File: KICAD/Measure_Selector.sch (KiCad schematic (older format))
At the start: 1 part

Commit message: merge program breaker nicolas
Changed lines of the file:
@@
 	-1   0    0    -1
 $EndComp
-Wire Wire Line
-	4900 3800 5225 3800
-Wire Wire Line
-	4900 3900 5225 3900
-Wire Wire Line
-	4900 4100 5225 4100
-Wire Wire Line
-	4900 4200 5225 4200
 $Comp
 L power:GND #PWR?
@@
 Wire Wire Line
 	5250 4500 4850 4500
+Wire Wire Line
+	5250 3800 4900 3800
+Wire Wire Line
+	4900 3900 5250 3900
+Wire Wire Line
+	5250 4100 4900 4100
+Wire Wire Line
+	4900 4200 5250 4200
 $EndSCHEMATC

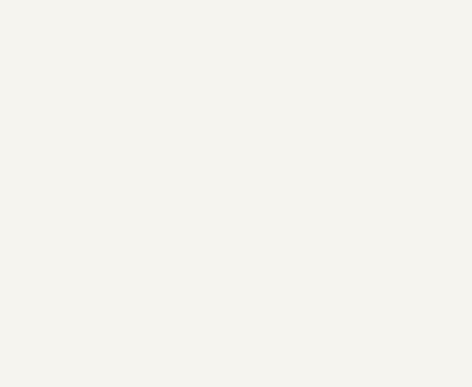
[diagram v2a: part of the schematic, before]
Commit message: added ramp draed by jebin + mod the current sim and it's working
!
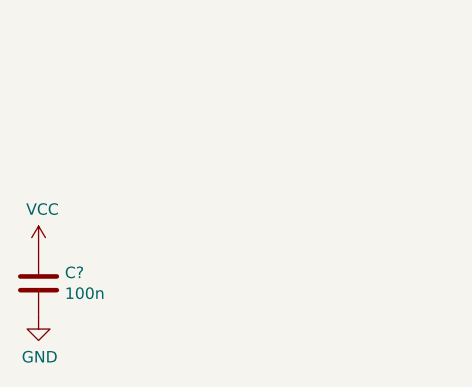
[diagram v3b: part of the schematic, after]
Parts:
- added C?: 100n, symbol Device:C
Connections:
- net GND: now also C?.2
- net VCC: now also C?.1
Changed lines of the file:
@@
-$EndComp
-$Comp
-L power:GND #PWR?
-U 1 1 610C24DF
-P 5800 4850
-F 0 "#PWR?" H 5800 4600 50  0001 C CNN
-F 1 "GND" H 5805 4677 50  0000 C CNN
-F 2 "" H 5800 4850 50  0001 C CNN
-F 3 "" H 5800 4850 50  0001 C CNN
-	1    5800 4850
-	1    0    0    -1
 $EndComp
 $Comp
@@
 Wire Wire Line
 	4900 4200 5250 4200
+$Comp
+L power:VCC #PWR?
+U 1 1 611208AC
+P 750 7150
+F 0 "#PWR?" H 750 7000 50  0001 C CNN
+F 1 "VCC" H 767 7323 50  0000 C CNN
+F 2 "" H 750 7150 50  0001 C CNN
+F 3 "" H 750 7150 50  0001 C CNN
+	1    750  7150
+	1    0    0    -1
+$EndComp
+$Comp
+L power:GND #PWR?
+U 1 1 610C24DF
+P 5800 4850
+F 0 "#PWR?" H 5800 4600 50  0001 C CNN
+F 1 "GND" H 5805 4677 50  0000 C CNN
+F 2 "" H 5800 4850 50  0001 C CNN
+F 3 "" H 5800 4850 50  0001 C CNN
+	1    5800 4850
+	1    0    0    -1
+$EndComp
+$Comp
+L power:GND #PWR?
+U 1 1 61122566
+P 750 7450
+F 0 "#PWR?" H 750 7200 50  0001 C CNN
+F 1 "GND" H 755 7277 50  0000 C CNN
+F 2 "" H 750 7450 50  0001 C CNN
+F 3 "" H 750 7450 50  0001 C CNN
+	1    750  7450
+	1    0    0    -1
+$EndComp
+$Comp
+L Device:C C?
+U 1 1 6112299E
+P 750 7300
+F 0 "C?" H 865 7346 50  0000 L CNN
+F 1 "100n" H 865 7255 50  0000 L CNN
+F 2 "" H 788 7150 50  0001 C CNN
+F 3 "~" H 750 7300 50  0001 C CNN
+	1    750  7300
+	1    0    0    -1
+$EndComp
 $EndSCHEMATC

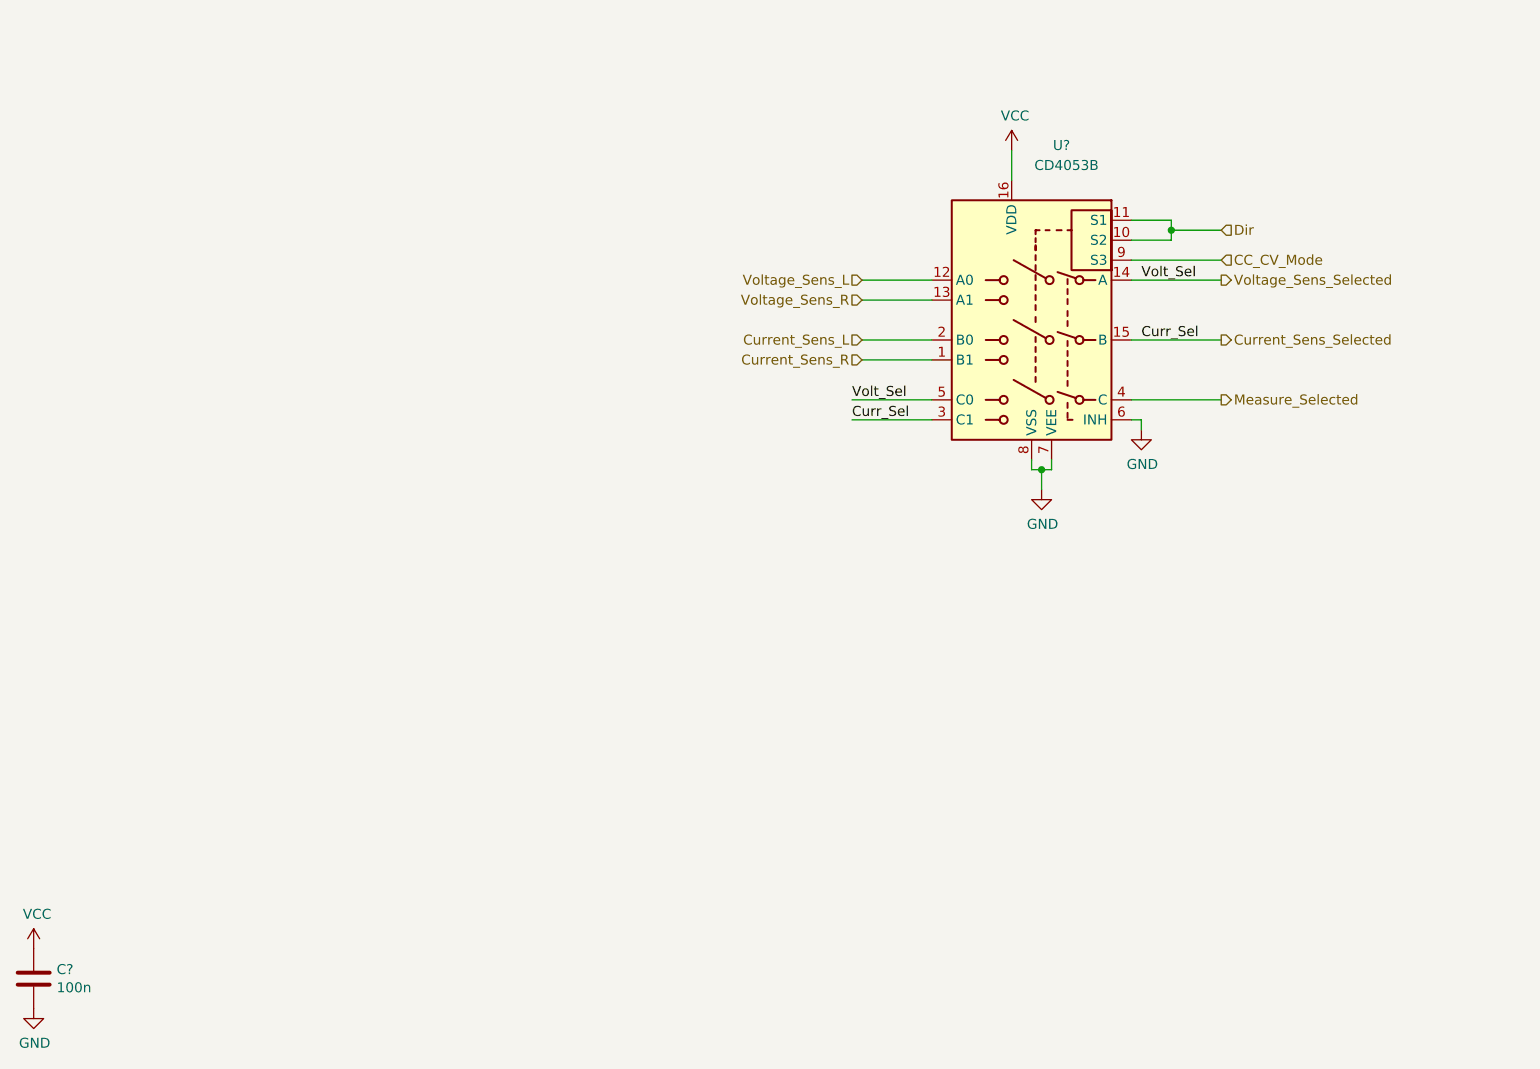
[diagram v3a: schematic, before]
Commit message: minors edits + 7v rail
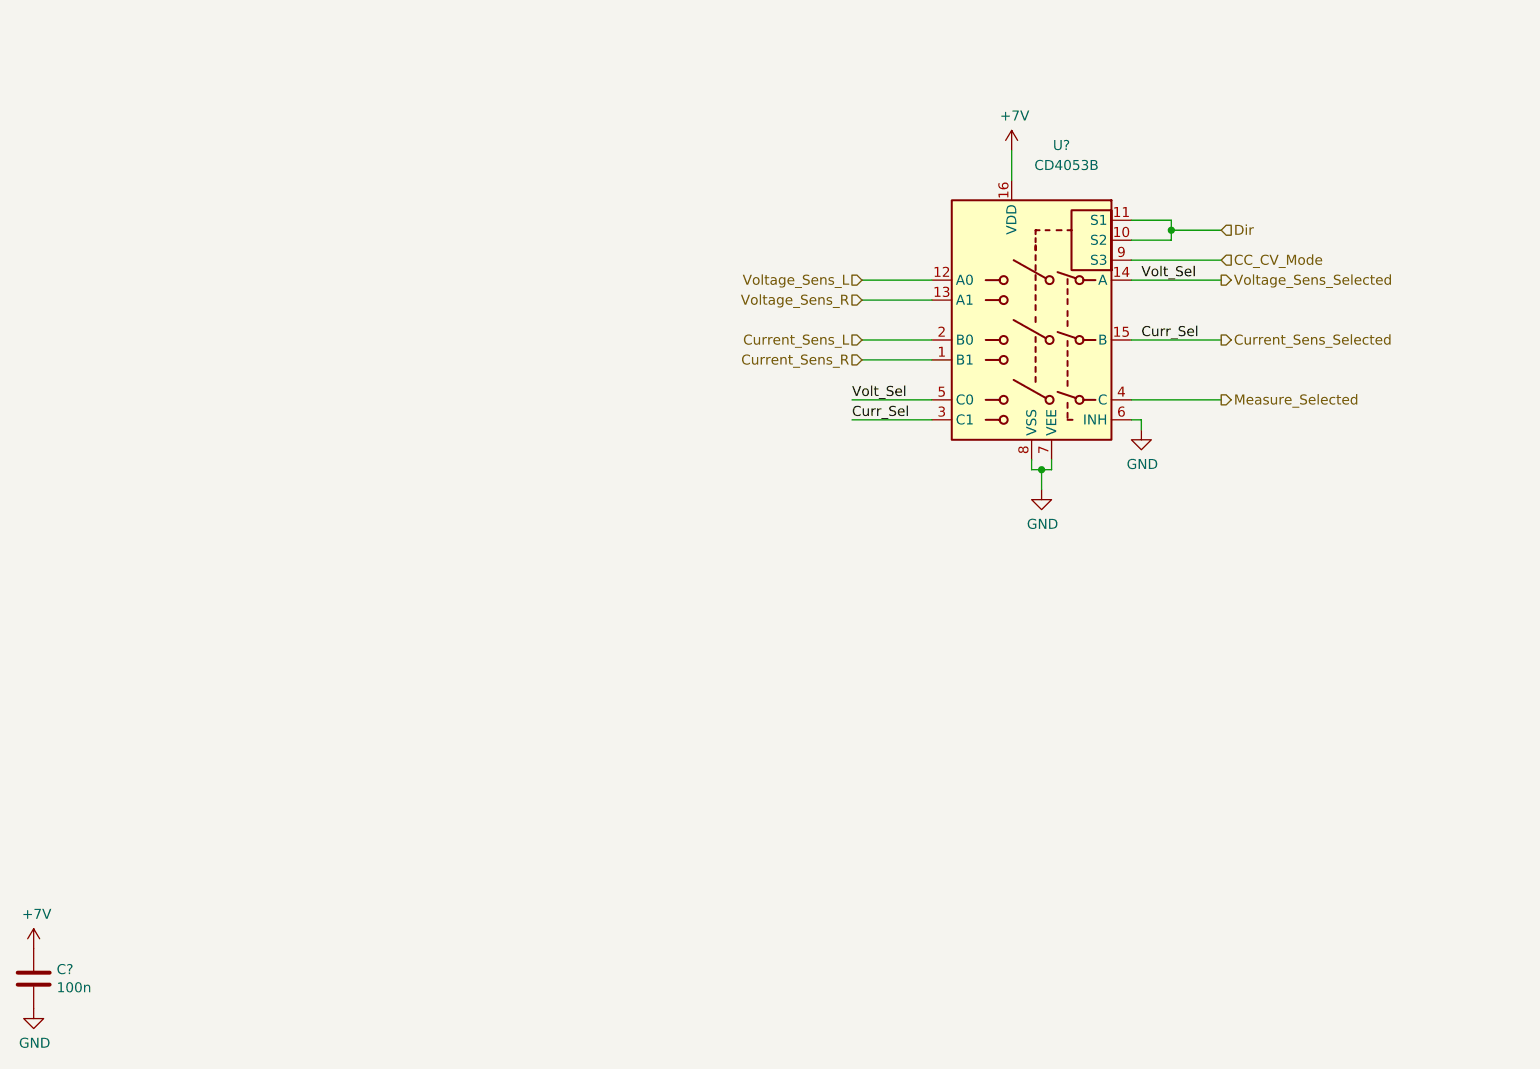
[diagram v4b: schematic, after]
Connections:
- net VCC renamed +7V
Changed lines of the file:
@@
 	-1   0    0    -1
-$EndComp
-$Comp
-L power:VCC #PWR?
-U 1 1 610C511E
-P 5650 3150
-F 0 "#PWR?" H 5650 3000 50  0001 C CNN
-F 1 "VCC" H 5667 3323 50  0000 C CNN
-F 2 "" H 5650 3150 50  0001 C CNN
-F 3 "" H 5650 3150 50  0001 C CNN
-	1    5650 3150
-	1    0    0    -1
 $EndComp
 Wire Wire Line
@@
 	4900 4200 5250 4200
 $Comp
-L power:VCC #PWR?
-U 1 1 611208AC
-P 750 7150
-F 0 "#PWR?" H 750 7000 50  0001 C CNN
-F 1 "VCC" H 767 7323 50  0000 C CNN
-F 2 "" H 750 7150 50  0001 C CNN
-F 3 "" H 750 7150 50  0001 C CNN
-	1    750  7150
-	1    0    0    -1
-$EndComp
-$Comp
 L power:GND #PWR?
 U 1 1 610C24DF
@@
 	1    0    0    -1
 $EndComp
+$Comp
+L Sesame:+7V #PWR?
+U 1 1 6128DF71
+P 5650 3150
+F 0 "#PWR?" H 5650 3000 50  0001 C CNN
+F 1 "+7V" H 5665 3323 50  0000 C CNN
+F 2 "" H 5650 3150 50  0001 C CNN
+F 3 "" H 5650 3150 50  0001 C CNN
+	1    5650 3150
+	1    0    0    -1
+$EndComp
+$Comp
+L Sesame:+7V #PWR?
+U 1 1 6128F549
+P 750 7150
+F 0 "#PWR?" H 750 7000 50  0001 C CNN
+F 1 "+7V" H 765 7323 50  0000 C CNN
+F 2 "" H 750 7150 50  0001 C CNN
+F 3 "" H 750 7150 50  0001 C CNN
+	1    750  7150
+	1    0    0    -1
+$EndComp

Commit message: a ton of new stuff. V0.8
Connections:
- net +7V renamed VCC
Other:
- moved on the sheet: U?
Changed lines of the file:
@@
 $Descr A4 11693 8268
 encoding utf-8
-Sheet 12 15
+Sheet 12 16
 Title "SESAME"
 Date "2021-08-03"
@@
 Comment4 ""
 $EndDescr
-Text HLabel 4900 3900 0    50   Input ~ 0
+Text HLabel 5250 3450 0    50   Input ~ 0
 Voltage_Sens_R
-Text HLabel 4900 4200 0    50   Input ~ 0
+Text HLabel 5250 3750 0    50   Input ~ 0
 Current_Sens_R
-Text HLabel 4900 3800 0    50   Input ~ 0
+Text HLabel 5250 3350 0    50   Input ~ 0
 Voltage_Sens_L
-Text HLabel 4900 4100 0    50   Input ~ 0
+Text HLabel 5250 3650 0    50   Input ~ 0
 Current_Sens_L
-Text HLabel 6700 3800 2    50   Output ~ 0
+Text HLabel 7050 3350 2    50   Output ~ 0
 Voltage_Sens_Selected
-Text HLabel 6700 4100 2    50   Output ~ 0
+Text HLabel 7050 3650 2    50   Output ~ 0
 Current_Sens_Selected
-Text HLabel 6700 3700 2    50   Input ~ 0
+Text HLabel 7050 3250 2    50   Input ~ 0
 CC_CV_Mode
-Text HLabel 6700 3550 2    50   Input ~ 0
+Text HLabel 7050 3100 2    50   Input ~ 0
 Dir
-Text HLabel 6700 4400 2    50   Output ~ 0
+Text HLabel 7050 3950 2    50   Output ~ 0
 Measure_Selected
 $Comp
 L sesame-fonctionnel-rescue:CD4053B-Analog_Switch U?
 U 1 1 610A09BD
-P 5750 4000
+P 6100 3550
 AR Path="/610A09BD" Ref="U?"  Part="1"
 AR Path="/60F421D1/610A09BD" Ref="U?"  Part="1"
-F 0 "U?" H 5600 4875 50  0000 C CNN
-F 1 "CD4053B" H 5575 4775 50  0000 C CNN
-F 2 "" H 5900 3250 50  0001 L CNN
-F 3 "http://www.ti.com/lit/ds/symlink/cd4052b.pdf" H 5730 4200 50  0001 C CNN
-	1    5750 4000
+F 0 "U?" H 5950 4425 50  0000 C CNN
+F 1 "CD4053B" H 5925 4325 50  0000 C CNN
+F 2 "" H 6250 2800 50  0001 L CNN
+F 3 "http://www.ti.com/lit/ds/symlink/cd4052b.pdf" H 6080 3750 50  0001 C CNN
+	1    6100 3550
 	-1   0    0    -1
 $EndComp
 Wire Wire Line
-	6250 3500 6450 3500
+	6600 3050 6800 3050
 Wire Wire Line
-	6450 3500 6450 3550
+	6800 3050 6800 3100
 Wire Wire Line
-	6450 3600 6250 3600
-Connection ~ 6450 3550
+	6800 3150 6600 3150
+Connection ~ 6800 3100
 Wire Wire Line
-	6450 3550 6450 3600
-Text Label 6300 3800 0    50   ~ 0
+	6800 3100 6800 3150
+Text Label 6650 3350 0    50   ~ 0
 Volt_Sel
-Text Label 6300 4100 0    50   ~ 0
+Text Label 6650 3650 0    50   ~ 0
 Curr_Sel
-Text Label 4850 4400 0    50   ~ 0
+Text Label 5200 3950 0    50   ~ 0
 Volt_Sel
-Text Label 4850 4500 0    50   ~ 0
+Text Label 5200 4050 0    50   ~ 0
 Curr_Sel
 $Comp
-L power:GND #PWR?
+L power:GND #PWR0161
 U 1 1 610E2D38
-P 6300 4550
-F 0 "#PWR?" H 6300 4300 50  0001 C CNN
-F 1 "GND" H 6305 4377 50  0000 C CNN
-F 2 "" H 6300 4550 50  0001 C CNN
-F 3 "" H 6300 4550 50  0001 C CNN
-	1    6300 4550
+P 6650 4100
+F 0 "#PWR0161" H 6650 3850 50  0001 C CNN
+F 1 "GND" H 6655 3927 50  0000 C CNN
+F 2 "" H 6650 4100 50  0001 C CNN
+F 3 "" H 6650 4100 50  0001 C CNN
+	1    6650 4100
 	1    0    0    -1
 $EndComp
 Wire Wire Line
-	6250 4500 6300 4500
+	6600 4050 6650 4050
 Wire Wire Line
-	6300 4500 6300 4550
+	6650 4050 6650 4100
 Wire Wire Line
-	5850 4700 5850 4750
+	6200 4250 6200 4300
 Wire Wire Line
-	5850 4750 5800 4750
+	6200 4300 6150 4300
 Wire Wire Line
-	5750 4750 5750 4700
+	6100 4300 6100 4250
 Wire Wire Line
-	5800 4750 5800 4850
-Connection ~ 5800 4750
+	6150 4300 6150 4400
+Connection ~ 6150 4300
 Wire Wire Line
-	5800 4750 5750 4750
+	6150 4300 6100 4300
 Wire Wire Line
-	6250 4400 6700 4400
+	6600 3950 7050 3950
 Wire Wire Line
-	6250 4100 6700 4100
+	6600 3650 7050 3650
 Wire Wire Line
-	6250 3800 6700 3800
+	6600 3350 7050 3350
 Wire Wire Line
-	6250 3700 6700 3700
+	6600 3250 7050 3250
 Wire Wire Line
-	6450 3550 6700 3550
+	6800 3100 7050 3100
 Wire Wire Line
-	5650 3150 5650 3300
+	6000 2700 6000 2850
 Wire Wire Line
-	5250 4400 4850 4400
+	5600 3950 5200 3950
 Wire Wire Line
-	5250 4500 4850 4500
+	5600 4050 5200 4050
 Wire Wire Line
-	5250 3800 4900 3800
+	5600 3350 5250 3350
 Wire Wire Line
-	4900 3900 5250 3900
+	5250 3450 5600 3450
 Wire Wire Line
-	5250 4100 4900 4100
+	5600 3650 5250 3650
 Wire Wire Line
-	4900 4200 5250 4200
+	5250 3750 5600 3750
 $Comp
-L power:GND #PWR?
+L power:GND #PWR0162
 U 1 1 610C24DF
-P 5800 4850
-F 0 "#PWR?" H 5800 4600 50  0001 C CNN
-F 1 "GND" H 5805 4677 50  0000 C CNN
-F 2 "" H 5800 4850 50  0001 C CNN
-F 3 "" H 5800 4850 50  0001 C CNN
-	1    5800 4850
+P 6150 4400
+F 0 "#PWR0162" H 6150 4150 50  0001 C CNN
+F 1 "GND" H 6155 4227 50  0000 C CNN
+F 2 "" H 6150 4400 50  0001 C CNN
+F 3 "" H 6150 4400 50  0001 C CNN
+	1    6150 4400
 	1    0    0    -1
 $EndComp
 $Comp
-L power:GND #PWR?
+L power:GND #PWR0163
 U 1 1 61122566
 P 750 7450
-F 0 "#PWR?" H 750 7200 50  0001 C CNN
+F 0 "#PWR0163" H 750 7200 50  0001 C CNN
 F 1 "GND" H 755 7277 50  0000 C CNN
 F 2 "" H 750 7450 50  0001 C CNN
@@
 $EndComp
 $Comp
-L Sesame:+7V #PWR?
-U 1 1 6128DF71
-P 5650 3150
-F 0 "#PWR?" H 5650 3000 50  0001 C CNN
-F 1 "+7V" H 5665 3323 50  0000 C CNN
-F 2 "" H 5650 3150 50  0001 C CNN
-F 3 "" H 5650 3150 50  0001 C CNN
-	1    5650 3150
-	1    0    0    -1
-$EndComp
-$Comp
-L Sesame:+7V #PWR?
-U 1 1 6128F549
+L power:VCC #PWR0164
+U 1 1 61547D97
 P 750 7150
-F 0 "#PWR?" H 750 7000 50  0001 C CNN
-F 1 "+7V" H 765 7323 50  0000 C CNN
+F 0 "#PWR0164" H 750 7000 50  0001 C CNN
+F 1 "VCC" H 765 7323 50  0000 C CNN
 F 2 "" H 750 7150 50  0001 C CNN
 F 3 "" H 750 7150 50  0001 C CNN
@@
 	1    0    0    -1
 $EndComp
+$Comp
+L power:VCC #PWR0165
+U 1 1 61549B3F
+P 6000 2700
+F 0 "#PWR0165" H 6000 2550 50  0001 C CNN
+F 1 "VCC" H 6015 2873 50  0000 C CNN
+F 2 "" H 6000 2700 50  0001 C CNN
+F 3 "" H 6000 2700 50  0001 C CNN
+	1    6000 2700
+	1    0    0    -1
+$EndComp

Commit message: reworked driver command
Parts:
- U?: value CD4053B -> CD4053BM96; footprint (none) -> Package_SO:SO-16_3.9x9.9mm_P1.27mm
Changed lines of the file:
@@
 $Descr A4 11693 8268
 encoding utf-8
-Sheet 12 16
+Sheet 11 16
 Title "SESAME"
 Date "2021-08-03"
@@
 AR Path="/610A09BD" Ref="U?"  Part="1"
 AR Path="/60F421D1/610A09BD" Ref="U?"  Part="1"
-F 0 "U?" H 5950 4425 50  0000 C CNN
-F 1 "CD4053B" H 5925 4325 50  0000 C CNN
-F 2 "" H 6250 2800 50  0001 L CNN
+F 0 "U?" H 5800 4400 50  0000 C CNN
+F 1 "CD4053BM96" H 5800 4300 50  0000 C CNN
+F 2 "Package_SO:SO-16_3.9x9.9mm_P1.27mm" H 6250 2800 50  0001 L CNN
 F 3 "http://www.ti.com/lit/ds/symlink/cd4052b.pdf" H 6080 3750 50  0001 C CNN
 	1    6100 3550

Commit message: mainly footprints
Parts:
- gave numbers to parts that had none: 1
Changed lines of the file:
@@
 $Descr A4 11693 8268
 encoding utf-8
-Sheet 11 16
+Sheet 6 16
 Title "SESAME"
 Date "2021-08-03"
@@
 P 6100 3550
 AR Path="/610A09BD" Ref="U?"  Part="1"
-AR Path="/60F421D1/610A09BD" Ref="U?"  Part="1"
-F 0 "U?" H 5800 4400 50  0000 C CNN
+AR Path="/60F421D1/610A09BD" Ref="U3"  Part="1"
+F 0 "U3" H 5800 4400 50  0000 C CNN
 F 1 "CD4053BM96" H 5800 4300 50  0000 C CNN
 F 2 "Package_SO:SO-16_3.9x9.9mm_P1.27mm" H 6250 2800 50  0001 L CNN

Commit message: revex with jmt
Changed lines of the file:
@@
 $Descr A4 11693 8268
 encoding utf-8
-Sheet 6 16
+Sheet 5 16
 Title "SESAME"
 Date "2021-08-03"
@@
 Text HLabel 5250 3650 0    50   Input ~ 0
 Current_Sens_L
-Text HLabel 7050 3350 2    50   Output ~ 0
+Text HLabel 7150 3350 2    50   Output ~ 0
 Voltage_Sens_Selected
-Text HLabel 7050 3650 2    50   Output ~ 0
+Text HLabel 7150 3650 2    50   Output ~ 0
 Current_Sens_Selected
-Text HLabel 7050 3250 2    50   Input ~ 0
+Text HLabel 7150 3250 2    50   Input ~ 0
 CC_CV_Mode
-Text HLabel 7050 3100 2    50   Input ~ 0
+Text HLabel 7150 3100 2    50   Input ~ 0
 Dir
-Text HLabel 7050 3950 2    50   Output ~ 0
+Text HLabel 7150 3950 2    50   Output ~ 0
 Measure_Selected
 $Comp
@@
 Wire Wire Line
 	6800 3100 6800 3150
-Text Label 6650 3350 0    50   ~ 0
-Volt_Sel
-Text Label 6650 3650 0    50   ~ 0
-Curr_Sel
-Text Label 5200 3950 0    50   ~ 0
-Volt_Sel
-Text Label 5200 4050 0    50   ~ 0
-Curr_Sel
 $Comp
 L power:GND #PWR0161
@@
 	6150 4300 6100 4300
 Wire Wire Line
-	6600 3950 7050 3950
+	6600 3950 7150 3950
 Wire Wire Line
-	6600 3650 7050 3650
+	6600 3650 6850 3650
 Wire Wire Line
-	6600 3350 7050 3350
+	6600 3350 7000 3350
 Wire Wire Line
-	6600 3250 7050 3250
+	6600 3250 7150 3250
 Wire Wire Line
-	6800 3100 7050 3100
+	6800 3100 7150 3100
 Wire Wire Line
 	6000 2700 6000 2850
 Wire Wire Line
-	5600 3950 5200 3950
+	5600 3950 5400 3950
 Wire Wire Line
-	5600 4050 5200 4050
+	5600 4050 5500 4050
 Wire Wire Line
 	5600 3350 5250 3350
@@
 	1    0    0    -1
 $EndComp
+Wire Wire Line
+	6850 3650 6850 4700
+Wire Wire Line
+	6850 4700 5500 4700
+Wire Wire Line
+	5500 4700 5500 4050
+Connection ~ 6850 3650
+Wire Wire Line
+	6850 3650 7150 3650
+Wire Wire Line
+	5400 3950 5400 4800
+Wire Wire Line
+	5400 4800 7000 4800
+Wire Wire Line
+	7000 3350 7000 4800
+Connection ~ 7000 3350
+Wire Wire Line
+	7000 3350 7150 3350
 $EndSCHEMATC
